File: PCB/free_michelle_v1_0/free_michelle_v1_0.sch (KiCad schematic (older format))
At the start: 16 parts

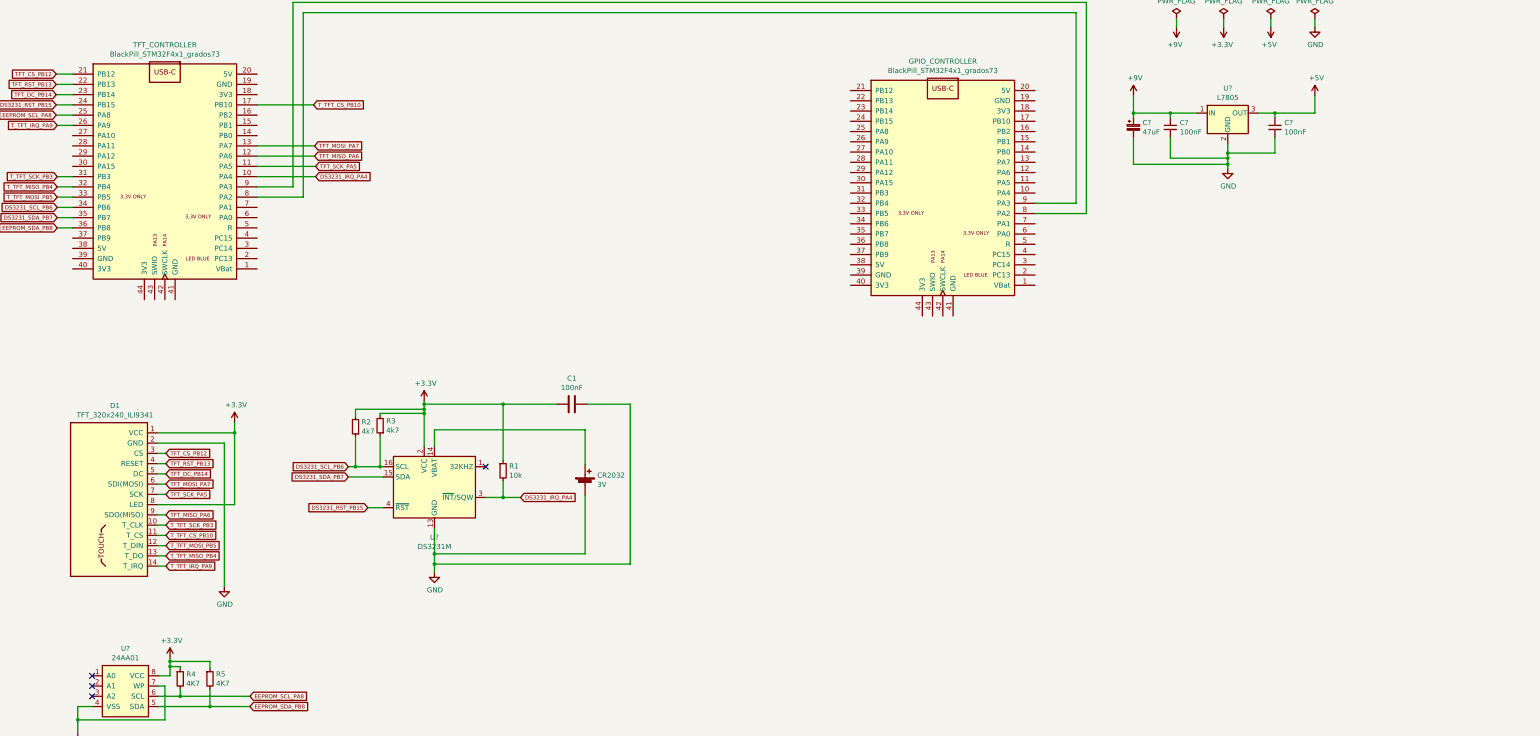
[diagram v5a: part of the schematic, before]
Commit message: Dodany LD1117V33
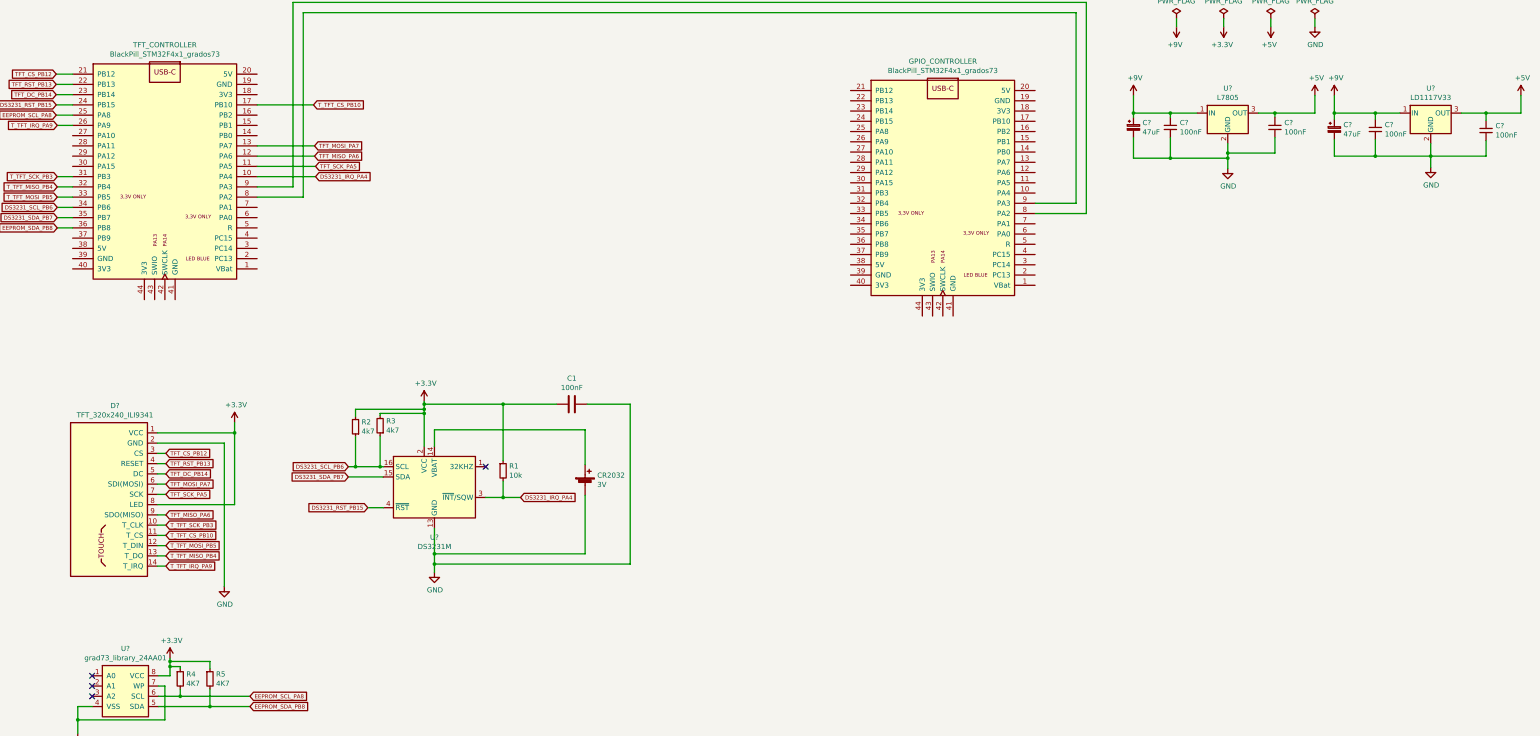
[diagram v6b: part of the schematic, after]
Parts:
- removed D1: TFT_320x240_ILI9341, symbol grad73_library:TFT_320x240_ILI9341
- removed U?: 24AA01, symbol grad73_library:24AA01
- added C?: 47uF, symbol Device:CP_Small
- added C? (x2): 100nF, symbol Device:C_Small
- added D?: TFT_320x240_ILI9341, symbol grad73_library:TFT_320x240_ILI9341
- added U?: LD1117V33, symbol grad73_library:LD1117V33
- added U?: grad73_library_24AA01, symbol free_michelle_v1_0-cache:grad73_library_24AA01
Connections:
- net +3V3: now also D?.1 (VCC), D?.8 (LED), U?.8 (VCC)
- net +5V: now also C?.1, U?.3 (OUT)
- net +9V: now also C?.1, C?.1, U?.1 (IN)
- net EEPROM_SCL_PA8: now also U?.6 (SCL)
- net EEPROM_SDA_PB8: now also U?.5 (SDA)
- net GND: now also C?.2, C?.2, C?.2, D?.2 (GND), U?.2 (GND), U?.4 (VSS), U?.7 (WP)
- net TFT_CS_PB12: now also D?.3 (CS)
- net TFT_DC_PB14: now also D?.5 (DC)
- net TFT_MISO_PA6: now also D?.9 (SDO(MISO))
- net TFT_MOSI_PA7: now also D?.6 (SDI(MOSI))
- net TFT_RST_PB13: now also D?.4 (RESET)
- net TFT_SCK_PA5: now also D?.7 (SCK)
- net T_TFT_CS_PB10: now also D?.11 (T_CS)
- net T_TFT_IRQ_PA9: now also D?.14 (T_IRQ)
- net T_TFT_MISO_PB4: now also D?.13 (T_DO)
- net T_TFT_MOSI_PB5: now also D?.12 (T_DIN)
- net T_TFT_SCK_PB3: now also D?.10 (T_CLK)
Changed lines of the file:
@@
 	11640 2960 11140 2960
-$Comp
-L grad73_library:TFT_320x240_ILI9341 D1
-U 1 1 61DB7F28
-P 2430 4900
-F 0 "D1" H 2163 4965 50  0000 C CNN
-F 1 "TFT_320x240_ILI9341" H 2163 4874 50  0000 C CNN
-F 2 "" H 2430 4900 50  0001 C CNN
-F 3 "" H 2430 4900 50  0001 C CNN
-	1    2430 4900
-	1    0    0    -1
-$EndComp
 $Comp
 L power:GND #PWR?
@@
 	4750 5430 4780 5430
 $Comp
-L grad73_library:24AA01 U?
-U 1 1 61DD6889
-P 2240 7320
-F 0 "U?" H 2265 7435 50  0000 C CNN
-F 1 "24AA01" H 2265 7344 50  0000 C CNN
-F 2 "" H 2240 7320 50  0001 C CNN
-F 3 "" H 2240 7320 50  0001 C CNN
-	1    2240 7320
-	1    0    0    -1
-$EndComp
-$Comp
 L power:GND #PWR?
 U 1 1 61DD74E4
@@
 	1    0    0    -1
 $EndComp
-Wire Wire Line
-	13020 2520 13020 2480
 $Comp
 L power:+9V #PWR?
@@
 	12460 1980 12720 1980
 Wire Wire Line
-	12100 2220 12100 2480
-Wire Wire Line
-	12100 2480 13020 2480
-Connection ~ 13020 2480
-Wire Wire Line
-	13020 2480 13020 2420
-Wire Wire Line
 	12460 2220 12460 2420
 Wire Wire Line
@@
 Wire Wire Line
 	13020 2370 13020 2280
+$Comp
+L grad73_library:LD1117V33 U?
+U 1 1 61E4A9E3
+P 15000 1980
+F 0 "U?" H 15000 2222 50  0000 C CNN
+F 1 "LD1117V33" H 15000 2131 50  0000 C CNN
+F 2 "" H 15025 1830 50  0001 L CIN
+F 3 "" H 15000 1930 50  0001 C CNN
+	1    15000 1980
+	1    0    0    -1
+$EndComp
+$Comp
+L free_michelle_v1_0-cache:grad73_library_24AA01 U?
+U 1 1 61E51F54
+P 2240 7320
+F 0 "U?" H 2265 7435 50  0000 C CNN
+F 1 "grad73_library_24AA01" H 2265 7344 50  0000 C CNN
+F 2 "" H 2240 7320 50  0001 C CNN
+F 3 "" H 2240 7320 50  0001 C CNN
+	1    2240 7320
+	1    0    0    -1
+$EndComp
+$Comp
+L grad73_library:TFT_320x240_ILI9341 D?
+U 1 1 61E56922
+P 2430 4900
+F 0 "D?" H 2163 4965 50  0000 C CNN
+F 1 "TFT_320x240_ILI9341" H 2163 4874 50  0000 C CNN
+F 2 "" H 2430 4900 50  0001 C CNN
+F 3 "" H 2430 4900 50  0001 C CNN
+	1    2430 4900
+	1    0    0    -1
+$EndComp
+$Comp
+L power:+9V #PWR?
+U 1 1 61E6D4C2
+P 14060 1810
+F 0 "#PWR?" H 14060 1660 50  0001 C CNN
+F 1 "+9V" H 14075 1983 50  0000 C CNN
+F 2 "" H 14060 1810 50  0001 C CNN
+F 3 "" H 14060 1810 50  0001 C CNN
+	1    14060 1810
+	1    0    0    -1
+$EndComp
+$Comp
+L power:+5V #PWR?
+U 1 1 61E6E504
+P 15880 1810
+F 0 "#PWR?" H 15880 1660 50  0001 C CNN
+F 1 "+5V" H 15895 1983 50  0000 C CNN
+F 2 "" H 15880 1810 50  0001 C CNN
+F 3 "" H 15880 1810 50  0001 C CNN
+	1    15880 1810
+	1    0    0    -1
+$EndComp
+$Comp
+L power:GND #PWR?
+U 1 1 61E6EB78
+P 15000 2510
+F 0 "#PWR?" H 15000 2260 50  0001 C CNN
+F 1 "GND" H 15005 2337 50  0000 C CNN
+F 2 "" H 15000 2510 50  0001 C CNN
+F 3 "" H 15000 2510 50  0001 C CNN
+	1    15000 2510
+	1    0    0    -1
+$EndComp
+Wire Wire Line
+	14060 1810 14060 1980
+Wire Wire Line
+	14060 1980 14460 1980
+Wire Wire Line
+	15300 1980 15540 1980
+Wire Wire Line
+	15880 1980 15880 1810
+Wire Wire Line
+	15000 2510 15000 2400
+$Comp
+L Device:CP_Small C?
+U 1 1 61E7B8D4
+P 14060 2140
+F 0 "C?" H 14148 2186 50  0000 L CNN
+F 1 "47uF" H 14148 2095 50  0000 L CNN
+F 2 "" H 14060 2140 50  0001 C CNN
+F 3 "~" H 14060 2140 50  0001 C CNN
+	1    14060 2140
+	1    0    0    -1
+$EndComp
+$Comp
+L Device:C_Small C?
+U 1 1 61E7BEE4
+P 14460 2140
+F 0 "C?" H 14552 2186 50  0000 L CNN
+F 1 "100nF" H 14552 2095 50  0000 L CNN
+F 2 "" H 14460 2140 50  0001 C CNN
+F 3 "~" H 14460 2140 50  0001 C CNN
+	1    14460 2140
+	1    0    0    -1
+$EndComp
+$Comp
+L Device:C_Small C?
+U 1 1 61E7C508
+P 15540 2150
+F 0 "C?" H 15632 2196 50  0000 L CNN
+F 1 "100nF" H 15632 2105 50  0000 L CNN
+F 2 "" H 15540 2150 50  0001 C CNN
+F 3 "~" H 15540 2150 50  0001 C CNN
+	1    15540 2150
+	1    0    0    -1
+$EndComp
+Wire Wire Line
+	13020 2420 13020 2520
+Wire Wire Line
+	12100 2220 12100 2420
+Wire Wire Line
+	12100 2420 12460 2420
+Connection ~ 12460 2420
+Wire Wire Line
+	14060 2040 14060 1980
+Connection ~ 14060 1980
+Wire Wire Line
+	14060 2240 14060 2400
+Wire Wire Line
+	14060 2400 14460 2400
+Connection ~ 15000 2400
+Wire Wire Line
+	15000 2400 15000 2280
+Wire Wire Line
+	14460 2240 14460 2400
+Connection ~ 14460 2400
+Wire Wire Line
+	14460 2400 15000 2400
+Wire Wire Line
+	14460 2040 14460 1980
+Connection ~ 14460 1980
+Wire Wire Line
+	14460 1980 14700 1980
+Wire Wire Line
+	15000 2400 15540 2400
+Wire Wire Line
+	15540 2400 15540 2250
+Wire Wire Line
+	15540 2050 15540 1980
+Connection ~ 15540 1980
+Wire Wire Line
+	15540 1980 15880 1980
 $EndSCHEMATC

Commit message: Dodane zasialnie i zlacza do programwoania
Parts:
- added J? (x2): SW, symbol Connector:Conn_01x04_Male
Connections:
- net +3V3: now also C?.1, GPIO_CONTROLLER.18 (3V3), GPIO_CONTROLLER.40 (3V3), GPIO_CONTROLLER.44 (3V3), TFT_CONTROLLER.18 (3V3), TFT_CONTROLLER.40 (3V3), TFT_CONTROLLER.44 (3V3), U?.3 (OUT), J?.1 (Pin_1), J?.1 (Pin_1)
- net +5V: no longer C?.1, U?.3 (OUT)
- net GND: now also GPIO_CONTROLLER.19 (GND), GPIO_CONTROLLER.39 (GND), GPIO_CONTROLLER.41 (GND), TFT_CONTROLLER.19 (GND), TFT_CONTROLLER.39 (GND), TFT_CONTROLLER.41 (GND), J?.4 (Pin_4), J?.4 (Pin_4)
- net at TFT_CONTROLLER.42 (SWCLK): now also J?.3 (Pin_3)
- net at TFT_CONTROLLER.43 (SWIO): now also J?.2 (Pin_2)
- net at GPIO_CONTROLLER.42 (SWCLK): now also J?.3 (Pin_3)
- net at GPIO_CONTROLLER.43 (SWIO): now also J?.2 (Pin_2)
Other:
- moved on the sheet: C1, CR2032, D?, R1, R2, R3, R4, R5, U?

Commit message: Dodane WS2812b
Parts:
- added J?: WS2812b, symbol Connector:Conn_01x03_Male
- added Q?: BSS138, Package_TO_SOT_SMD:SOT-23, symbol Transistor_FET:BSS138
- added R? (x3): 4k7, symbol Device:R_Small
- added U?: BMP280, symbol grad73_library:BMP280
- U?: value grad73_library_24AA01 -> EEPROM_24AA01
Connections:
- net +3V3: now also R?.2, R?.2, U?.1 (VCC)
- net +5V: now also R?.2
- net GND: now also J?.1 (Pin_1), U?.2 (GND)
- net BMP_SCL_PB8: now reaches GPIO_CONTROLLER.36 (PB8)
- net BMP_SCL_PB8: now also U?.3 (SCL)
- net BMP_SDA_PB9: now reaches GPIO_CONTROLLER.37 (PB9)
- net BMP_SDA_PB9: now also U?.4 (SDA)
- new net: J?.2 (Pin_2), Q?.3 (D), R?.1
- new net: Q?.1 (G), R?.1
- new net +5VP: J?.3 (Pin_3)
- new net WS2812b_PA9: Q?.2 (S), R?.1
- no-connect marks 4 -> 6
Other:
- note added: "LOGIKI 3,3V"
- note added: "LOGIKI 5V"
- note added: "NAPIĘCIE ZASILANIA"
- note added: "O WYSOKIEJ WYDAJNOŚCI"
- note added: "PRĄDOWEJ"
- note added: "WEJŚCIOWE"
